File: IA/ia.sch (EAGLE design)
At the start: 20 parts, among them IC1 7805TV

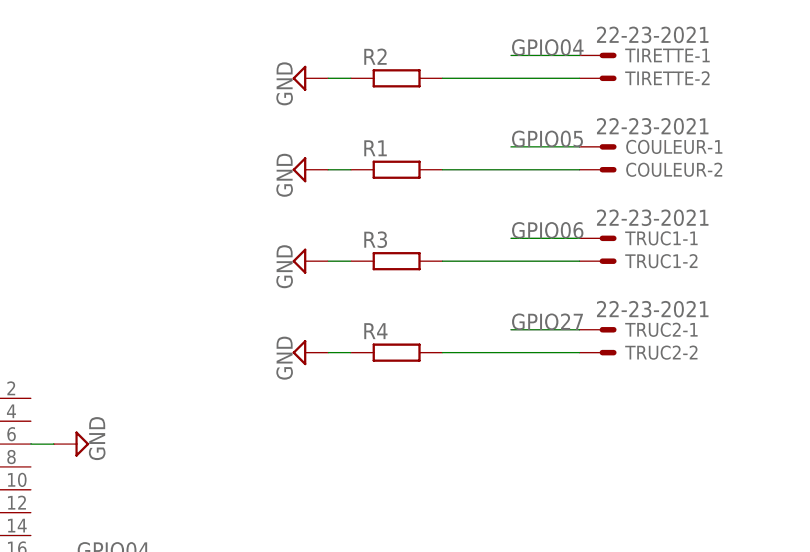
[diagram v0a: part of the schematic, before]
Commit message: IA: Correction des pullup sur les GPIOs
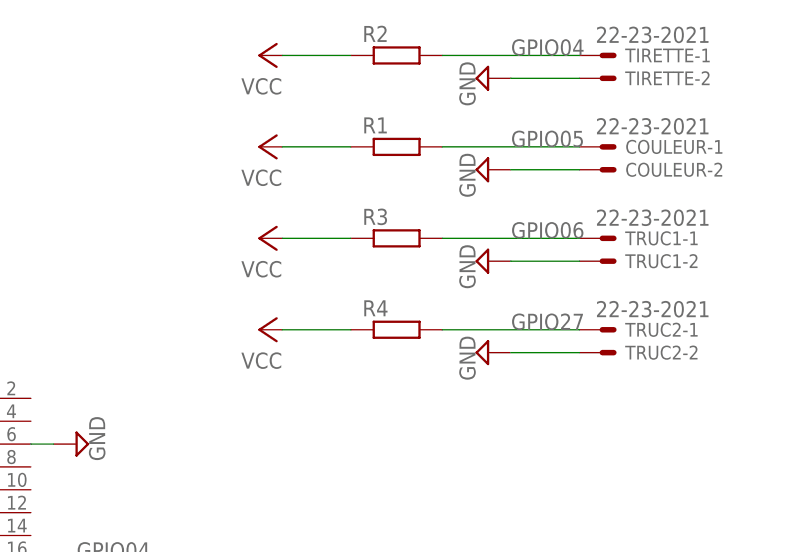
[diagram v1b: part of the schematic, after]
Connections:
- removed net N$10: R2.2, TIRETTE-2.S
- removed net N$11: COULEUR-2.S, R1.2
- removed net N$12: R3.2, TRUC1-2.S
- removed net N$13: R4.2, TRUC2-2.S
- net GND: now also COULEUR-2.S, TIRETTE-2.S, TRUC1-2.S, TRUC2-2.S; no longer R1.1, R2.1, R3.1, R4.1
- net GPIO04: now also R2.2
- net GPIO05: now also R1.2
- net GPIO06: now also R3.2
- net GPIO27: now also R4.2
- net VCC: now also R1.1, R2.1, R3.1, R4.1
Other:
- moved on the sheet: R1, R2, R3, R4

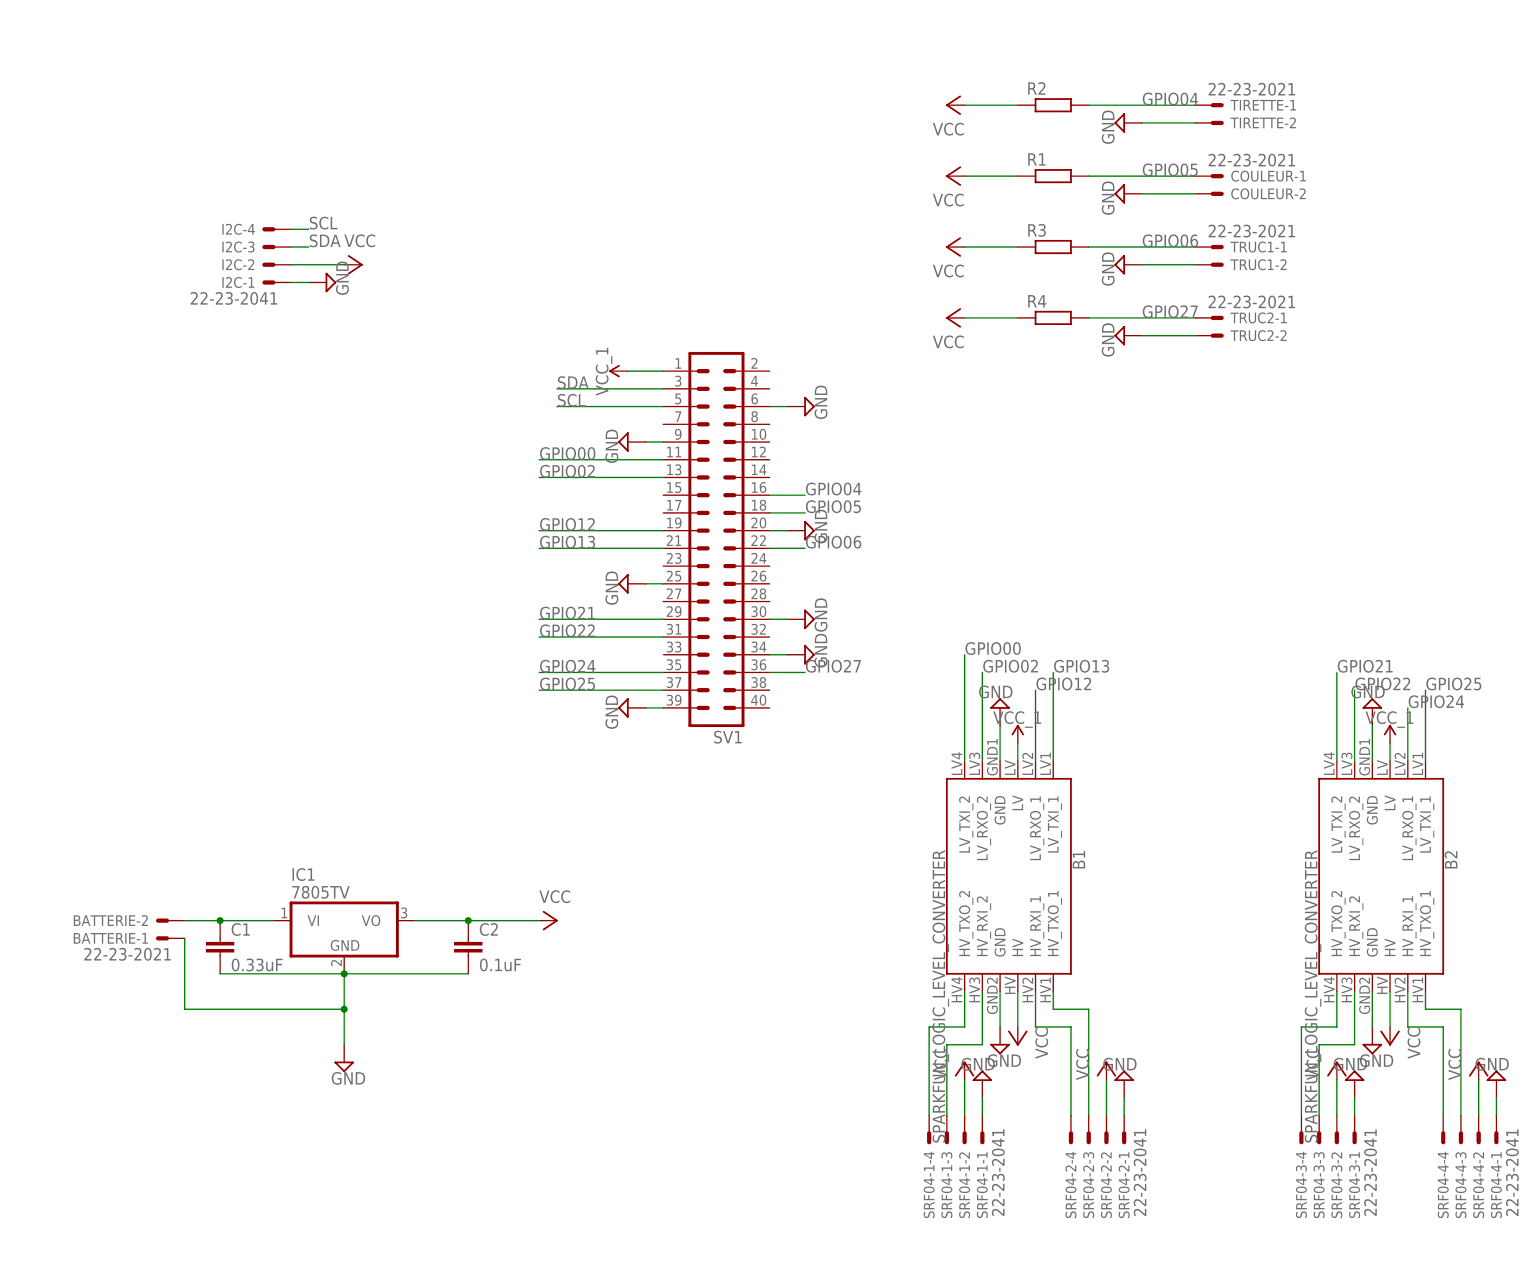
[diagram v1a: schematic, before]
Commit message: puissance IA + carte AX12
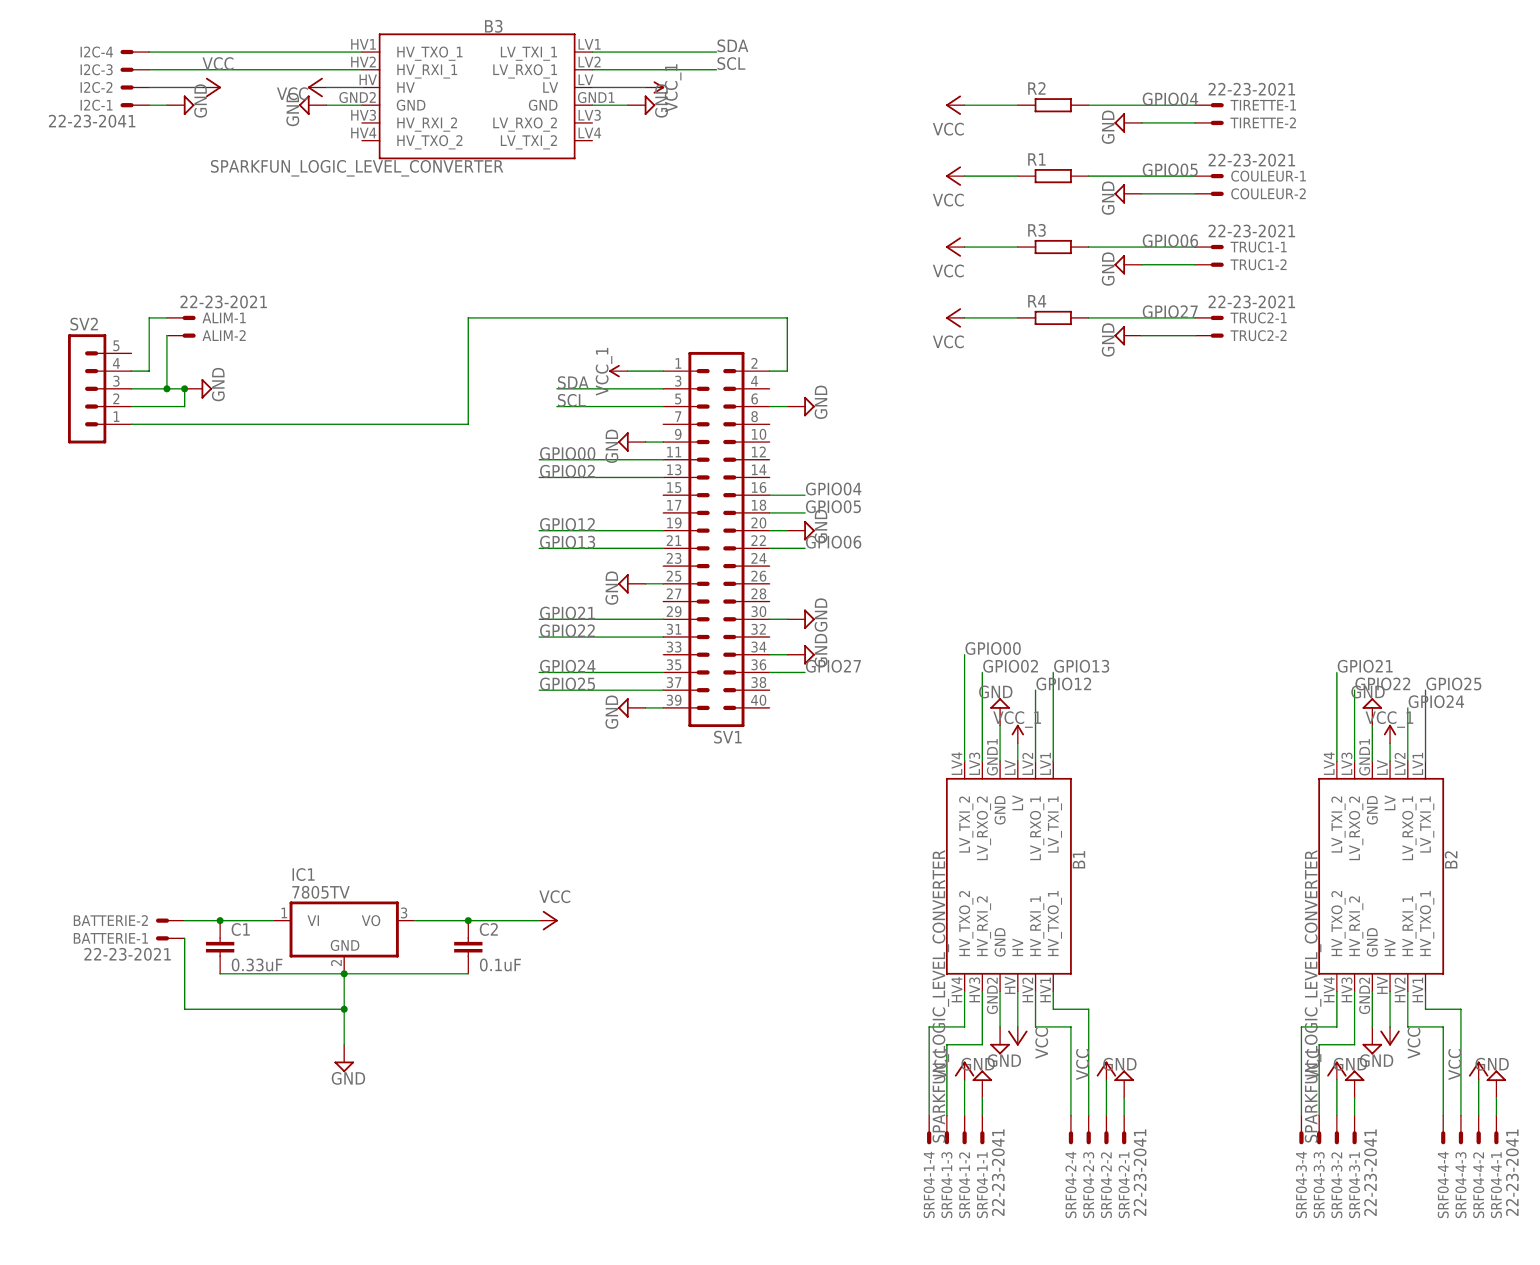
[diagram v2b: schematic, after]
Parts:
- added ALIM: 22-23-2021, con-molex:22-23-2021
- added B3: SPARKFUN_LOGIC_LEVEL_CONVERTER, SparkFun-Boards:SPARKFUN_LOGIC_LEVEL_CONVERTER
- added SV2: (no value), con-lstb:MA05-1
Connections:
- new net N$10: B3.HV_RXI_1, I2C-3.S
- new net N$11: B3.HV_TXO_1, I2C-4.S
- new net N$13: SV1.2, SV2.1
- new net N$14: ALIM-1.S, SV2.4
- net GND: now also ALIM-2.S, B3.GND, B3.GND@2, SV2.2, SV2.3
- net SCL: now also B3.LV_RXO_1; no longer I2C-4.S
- net SDA: now also B3.LV_TXI_1; no longer I2C-3.S
- net VCC: now also B3.HV
- net VCC_1: now also B3.LV
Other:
- moved on the sheet: I2C-1, I2C-2, I2C-3, I2C-4
